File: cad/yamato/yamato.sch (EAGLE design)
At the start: 2 parts, among them IC1 ULN2003AN

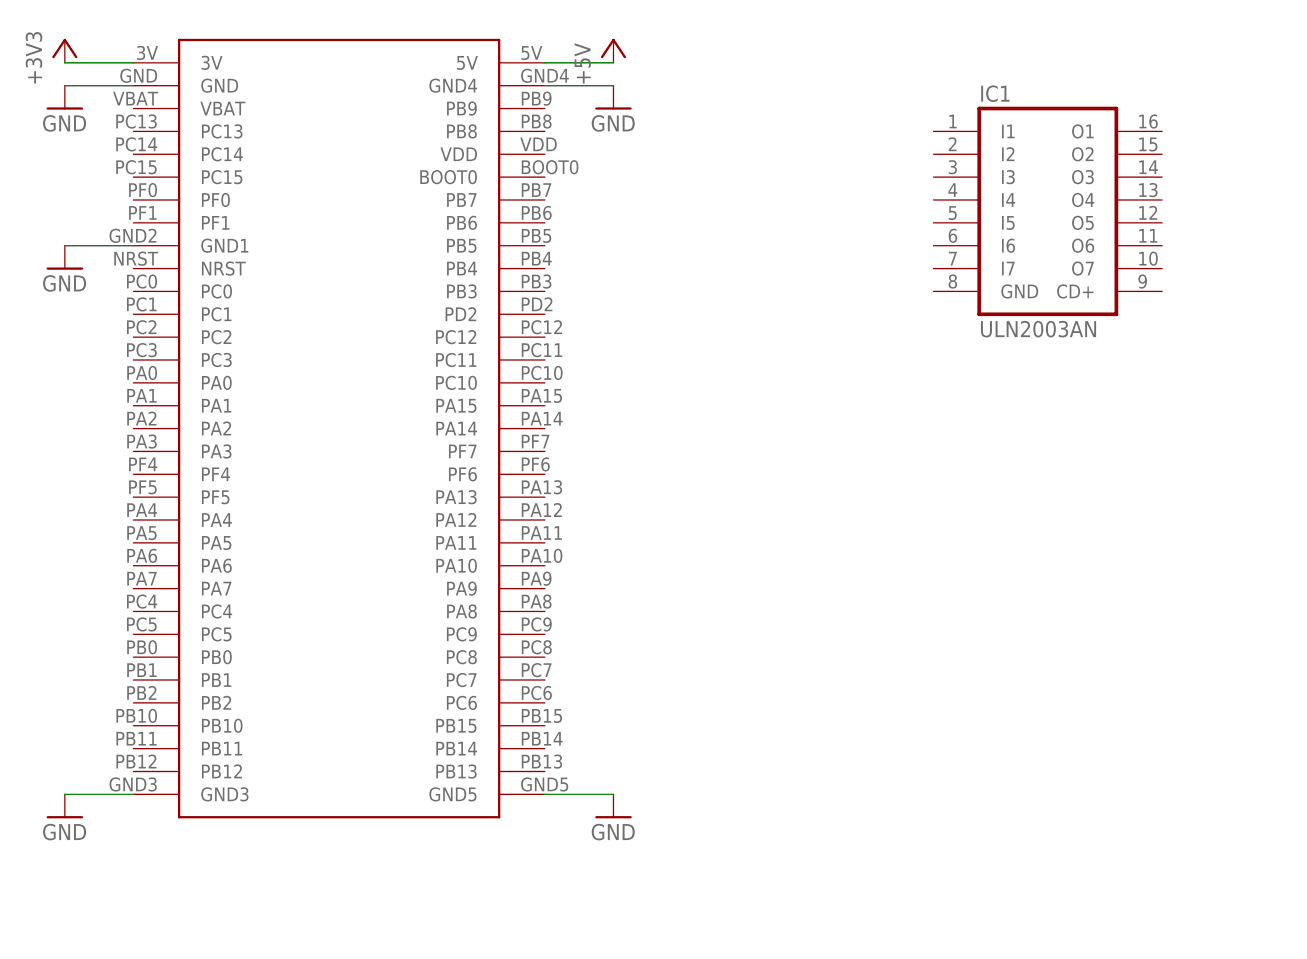
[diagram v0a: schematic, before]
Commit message: Remove dynamic threads
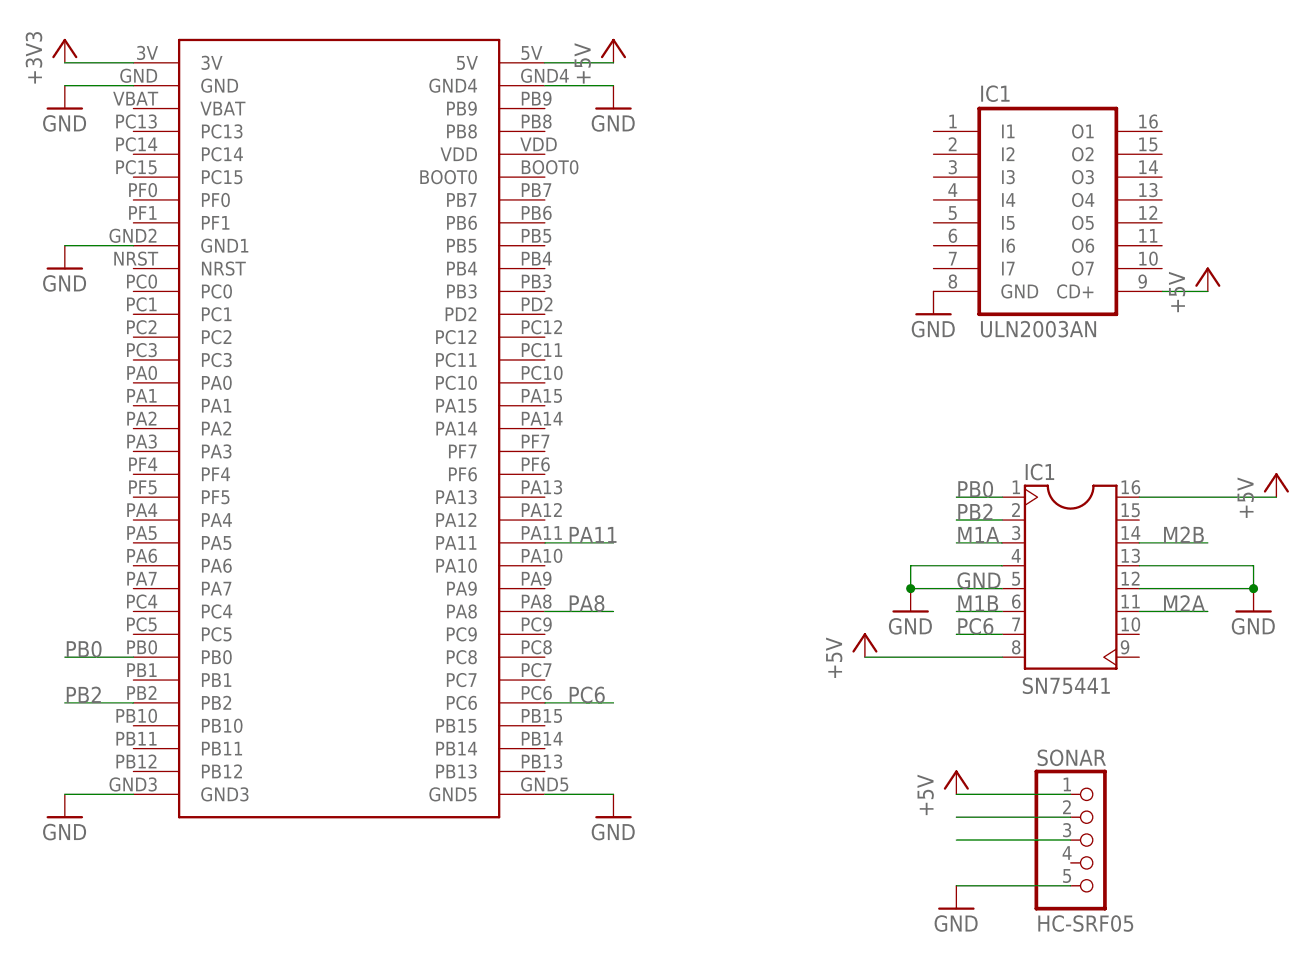
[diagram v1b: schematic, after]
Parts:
- added SONAR: HC-SRF05, pinhead:PINHD-1X5
- added U$2: SN75441-DEVICESN75411-SOCKET, yamato:SN75441-DEVICESN75411-SOCKET
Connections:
- new net M1A: U$2.1Y
- new net M1B: U$2.2Y
- new net M2A: U$2.3Y
- new net M2B: U$2.4Y
- new net PA11: SONAR.2, U$1.PA11
- new net PA8: SONAR.3, U$1.PA8
- new net PB0: U$1.PB0, U$2.12EN
- new net PB2: U$1.PB2, U$2.1A
- new net PC6: U$1.PC6, U$2.2A
- net +5V: now also IC1.CD+, SONAR.1, U$2.VCC1, U$2.VCC2
- net GND: now also IC1.GND, SONAR.5, U$2.GND, U$2.GND1, U$2.GND2, U$2.GND3
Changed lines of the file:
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@@
 <part name="+3V1" library="supply1" deviceset="+3V3" device=""/>
 <part name="P+1" library="supply1" deviceset="+5V" device=""/>
+<part name="P+2" library="supply1" deviceset="+5V" device=""/>
+<part name="GND6" library="supply1" deviceset="GND" device=""/>
+<part name="U$2" library="yamato" deviceset="SN75441-DEVICE" device="SN75411-SOCKET"/>
+<part name="P+3" library="supply1" deviceset="+5V" device=""/>
+<part name="P+4" library="supply1" deviceset="+5V" device=""/>
+<part name="GND7" library="supply1" deviceset="GND" device=""/>
+<part name="GND8" library="supply1" deviceset="GND" device=""/>
+<part name="SONAR" library="pinhead" deviceset="PINHD-1X5" device="" value="HC-SRF05"/>
+<part name="P+5" library="supply1" deviceset="+5V" device=""/>
+<part name="GND9" library="supply1" deviceset="GND" device=""/>
 </parts>
 <sheets>
@@
 <instance part="+3V1" gate="G$1" x="-30.48" y="40.64"/>
 <instance part="P+1" gate="1" x="30.48" y="40.64"/>
+<instance part="P+2" gate="1" x="96.52" y="15.24"/>
+<instance part="GND6" gate="1" x="66.04" y="10.16"/>
+<instance part="U$2" gate="G$1" x="81.28" y="-17.78"/>
+<instance part="P+3" gate="1" x="58.42" y="-25.4"/>
+<instance part="P+4" gate="1" x="104.14" y="-7.62"/>
+<instance part="GND7" gate="1" x="63.5" y="-22.86"/>
+<instance part="GND8" gate="1" x="101.6" y="-22.86"/>
+<instance part="SONAR" gate="A" x="83.82" y="-48.26"/>
+<instance part="P+5" gate="1" x="68.58" y="-40.64"/>
+<instance part="GND9" gate="1" x="68.58" y="-55.88"/>
 </instances>
 <busses>
@@
 <wire x1="30.48" y1="35.56" x2="22.86" y2="35.56" width="0.1524" layer="91"/>
 </segment>
+<segment>
+<pinref part="IC1" gate="A" pin="GND"/>
+<pinref part="GND6" gate="1" pin="GND"/>
+</segment>
+<segment>
+<pinref part="U$2" gate="G$1" pin="GND"/>
+<pinref part="GND7" gate="1" pin="GND"/>
+<wire x1="73.66" y1="-17.78" x2="63.5" y2="-17.78" width="0.1524" layer="91"/>
+<wire x1="63.5" y1="-17.78" x2="63.5" y2="-20.32" width="0.1524" layer="91"/>
+<pinref part="U$2" gate="G$1" pin="GND1"/>
+<wire x1="73.66" y1="-20.32" x2="63.5" y2="-20.32" width="0.1524" layer="91"/>
+<junction x="63.5" y="-20.32"/>
+<label x="68.58" y="-20.32" size="1.778" layer="95"/>
+</segment>
+<segment>
+<pinref part="U$2" gate="G$1" pin="GND3"/>
+<pinref part="GND8" gate="1" pin="GND"/>
+<wire x1="88.9" y1="-17.78" x2="101.6" y2="-17.78" width="0.1524" layer="91"/>
+<wire x1="101.6" y1="-17.78" x2="101.6" y2="-20.32" width="0.1524" layer="91"/>
+<pinref part="U$2" gate="G$1" pin="GND2"/>
+<wire x1="88.9" y1="-20.32" x2="101.6" y2="-20.32" width="0.1524" layer="91"/>
+<junction x="101.6" y="-20.32"/>
+</segment>
+<segment>
+<pinref part="SONAR" gate="A" pin="5"/>
+<wire x1="81.28" y1="-53.34" x2="68.58" y2="-53.34" width="0.1524" layer="91"/>
+<pinref part="GND9" gate="1" pin="GND"/>
+</segment>
 </net>
 <net name="+3V3" class="0">
@@
 </segment>
 </net>
+<net name="PA8" class="0">
+<segment>
+<pinref part="U$1" gate="G$1" pin="PA8"/>
+<wire x1="22.86" y1="-22.86" x2="30.48" y2="-22.86" width="0.1524" layer="91"/>
+<label x="25.4" y="-22.86" size="1.778" layer="95"/>
+</segment>
+<segment>
+<pinref part="SONAR" gate="A" pin="3"/>
+<wire x1="81.28" y1="-48.26" x2="68.58" y2="-48.26" width="0.1524" layer="91"/>
+</segment>
+</net>
 <net name="+5V" class="0">
+<segment>
+<pinref part="SONAR" gate="A" pin="1"/>
+<wire x1="81.28" y1="-43.18" x2="68.58" y2="-43.18" width="0.1524" layer="91"/>
+<pinref part="P+5" gate="1" pin="+5V"/>
+</segment>
 <segment>
 <pinref part="P+1" gate="1" pin="+5V"/>
@@
 <wire x1="30.48" y1="38.1" x2="22.86" y2="38.1" width="0.1524" layer="91"/>
 </segment>
-</net>
+<segment>
+<pinref part="P+2" gate="1" pin="+5V"/>
+<pinref part="IC1" gate="A" pin="CD+"/>
+<wire x1="96.52" y1="12.7" x2="91.44" y2="12.7" width="0.1524" layer="91"/>
+</segment>
+<segment>
+<pinref part="U$2" gate="G$1" pin="VCC1"/>
+<pinref part="P+4" gate="1" pin="+5V"/>
+<wire x1="88.9" y1="-10.16" x2="104.14" y2="-10.16" width="0.1524" layer="91"/>
+</segment>
+<segment>
+<pinref part="U$2" gate="G$1" pin="VCC2"/>
+<pinref part="P+3" gate="1" pin="+5V"/>
+<wire x1="73.66" y1="-27.94" x2="58.42" y2="-27.94" width="0.1524" layer="91"/>
+</segment>
+</net>
+<net name="PA11" class="0">
+<segment>
+<pinref part="U$1" gate="G$1" pin="PA11"/>
+<wire x1="22.86" y1="-15.24" x2="30.48" y2="-15.24" width="0.1524" layer="91"/>
+<label x="25.4" y="-15.24" size="1.778" layer="95"/>
+</segment>
+<segment>
+<pinref part="SONAR" gate="A" pin="2"/>
+<wire x1="81.28" y1="-45.72" x2="68.58" y2="-45.72" width="0.1524" layer="91"/>
+</segment>
+</net>
+<net name="PB0" class="0">
+<segment>
+<pinref part="U$1" gate="G$1" pin="PB0"/>
+<wire x1="-22.86" y1="-27.94" x2="-30.48" y2="-27.94" width="0.1524" layer="91"/>
+<label x="-30.48" y="-27.94" size="1.778" layer="95"/>
+</segment>
+<segment>
+<pinref part="U$2" gate="G$1" pin="12EN"/>
+<wire x1="73.66" y1="-10.16" x2="68.58" y2="-10.16" width="0.1524" layer="91"/>
+<label x="68.58" y="-10.16" size="1.778" layer="95"/>
+</segment>
+</net>
+<net name="PB2" class="0">
+<segment>
+<pinref part="U$1" gate="G$1" pin="PB2"/>
+<wire x1="-22.86" y1="-33.02" x2="-30.48" y2="-33.02" width="0.1524" layer="91"/>
+<label x="-30.48" y="-33.02" size="1.778" layer="95"/>
+</segment>
+<segment>
+<pinref part="U$2" gate="G$1" pin="1A"/>
+<wire x1="73.66" y1="-12.7" x2="68.58" y2="-12.7" width="0.1524" layer="91"/>
+<label x="68.58" y="-12.7" size="1.778" layer="95"/>
+</segment>
+</net>
+<net name="PC6" class="0">
+<segment>
+<pinref part="U$1" gate="G$1" pin="PC6"/>
+<wire x1="22.86" y1="-33.02" x2="30.48" y2="-33.02" width="0.1524" layer="91"/>
+<label x="25.4" y="-33.02" size="1.778" layer="95"/>
+</segment>
+<segment>
+<pinref part="U$2" gate="G$1" pin="2A"/>
+<wire x1="73.66" y1="-25.4" x2="68.58" y2="-25.4" width="0.1524" layer="91"/>
+<label x="68.58" y="-25.4" size="1.778" layer="95"/>
+</segment>
+</net>
+<net name="M1A" class="0">
+<segment>
+<pinref part="U$2" gate="G$1" pin="1Y"/>
+<wire x1="73.66" y1="-15.24" x2="68.58" y2="-15.24" width="0.1524" layer="91"/>
+<label x="68.58" y="-15.24" size="1.778" layer="95"/>
+</segment>
+</net>
+<net name="M1B" class="0">
+<segment>
+<pinref part="U$2" gate="G$1" pin="2Y"/>
+<wire x1="73.66" y1="-22.86" x2="68.58" y2="-22.86" width="0.1524" layer="91"/>
+<label x="68.58" y="-22.86" size="1.778" layer="95"/>
+</segment>
+</net>
+<net name="M2B" class="0">
+<segment>
+<pinref part="U$2" gate="G$1" pin="4Y"/>
+<wire x1="88.9" y1="-15.24" x2="96.52" y2="-15.24" width="0.1524" layer="91"/>
+<label x="91.44" y="-15.24" size="1.778" layer="95"/>
+</segment>
+</net>
+<net name="M2A" class="0">
+<segment>
+<pinref part="U$2" gate="G$1" pin="3Y"/>
+<wire x1="88.9" y1="-22.86" x2="96.52" y2="-22.86" width="0.1524" layer="91"/>
+<label x="91.44" y="-22.86" size="1.778" layer="95"/>
+</segment>
+</net>
